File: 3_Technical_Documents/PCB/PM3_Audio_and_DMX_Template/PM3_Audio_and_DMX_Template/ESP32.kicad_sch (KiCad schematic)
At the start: 21 parts, among them SW1 SW_Push, SW2 SW_Push, U1 ESP32-WROOM-32E

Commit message: layout complete
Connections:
- net DIN_1: now also U1.36 (IO22); no longer U1.37 (IO23)
- net DOUT_1: now also U1.37 (IO23); no longer U1.36 (IO22)
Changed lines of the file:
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@@
+		)
+	)
+	(global_label "DIN_1"
+		(shape input)
+		(at 68.58 105.41 0)
+		(fields_autoplaced yes)
+		(effects
+			(font
+				(size 1 1)
+			)
+			(justify left)
+		)
+		(property "Intersheetrefs" "${INTERSHEET_REFS}"
+			(at 75.1684 105.41 0)
+			(effects
+				(font
+					(size 1.27 1.27)
+				)
+				(justify left)
+				(hide yes)
+			)
 		)
 	)
@@
 		)
 	)
+	(global_label "DOUT_1"
+		(shape input)
+		(at 68.58 107.95 0)
+		(fields_autoplaced yes)
+		(effects
+			(font
+				(size 1 1)
+			)
+			(justify left)
+		)
+		(property "Intersheetrefs" "${INTERSHEET_REFS}"
+			(at 76.5017 107.95 0)
+			(effects
+				(font
+					(size 1.27 1.27)
+				)
+				(justify left)
+				(hide yes)
+			)
+		)
+	)
 	(global_label "BCLK_2"
 		(shape input)
@@
 		)
 	)
-	(global_label "DIN_1"
-		(shape input)
-		(at 68.58 107.95 0)
-		(fields_autoplaced yes)
-		(effects
-			(font
-				(size 1 1)
-			)
-			(justify left)
-		)
-		(property "Intersheetrefs" "${INTERSHEET_REFS}"
-			(at 75.1684 107.95 0)
-			(effects
-				(font
-					(size 1.27 1.27)
-				)
-				(justify left)
-				(hide yes)
-			)
-		)
-	)
 	(global_label "Rx"
 		(shape input)
@@
 		)
 	)
-	(global_label "DOUT_1"
-		(shape input)
-		(at 68.58 105.41 0)
-		(fields_autoplaced yes)
-		(effects
-			(font
-				(size 1 1)
-			)
-			(justify left)
-		)
-		(property "Intersheetrefs" "${INTERSHEET_REFS}"
-			(at 76.5017 105.41 0)
-			(effects
-				(font
-					(size 1.27 1.27)
-				)
-				(justify left)
-				(hide yes)
-			)
-		)
-	)
 	(global_label "LRCLK_1"
 		(shape input)
@@
 		)
 		(property "Description" "Push button switch, generic, two pins"
+			(at 228.6 49.53 0)
+			(effects
+				(font
+					(size 1.27 1.27)
+				)
+				(hide yes)
+			)
+		)
+		(property "Sim.Type" ""
 			(at 228.6 49.53 0)
 			(effects
@@
 			)
 		)
+		(property "Sim.Type" ""
+			(at 219.71 44.45 0)
+			(effects
+				(font
+					(size 1.27 1.27)
+				)
+				(hide yes)
+			)
+		)
 		(pin "1"
 		)
@@
 			)
 		)
+		(property "Sim.Type" ""
+			(at 266.7 48.26 0)
+			(effects
+				(font
+					(size 1.27 1.27)
+				)
+				(hide yes)
+			)
+		)
 		(pin "2"
 		)
@@
 			)
 		)
+		(property "Sim.Type" ""
+			(at 156.21 105.41 0)
+			(effects
+				(font
+					(size 1.27 1.27)
+				)
+				(hide yes)
+			)
+		)
 		(pin "2"
 		)
@@
 			)
 		)
+		(property "Sim.Type" ""
+			(at 81.28 92.71 0)
+			(effects
+				(font
+					(size 1.27 1.27)
+				)
+				(hide yes)
+			)
+		)
 		(pin "1"
 		)
@@
 			)
 		)
+		(property "Sim.Type" ""
+			(at 156.21 107.95 0)
+			(effects
+				(font
+					(size 1.27 1.27)
+				)
+				(hide yes)
+			)
+		)
 		(pin "2"
 		)
@@
 			)
 		)
+		(property "Sim.Type" ""
+			(at 156.21 99.06 0)
+			(effects
+				(font
+					(size 1.27 1.27)
+				)
+				(hide yes)
+			)
+		)
 		(pin "2"
 		)
@@
 			)
 		)
+		(property "Sim.Type" ""
+			(at 91.44 43.18 0)
+			(effects
+				(font
+					(size 1.27 1.27)
+				)
+				(hide yes)
+			)
+		)
 		(pin "1"
 		)
@@
 			)
 		)
+		(property "Sim.Type" ""
+			(at 219.71 54.61 0)
+			(effects
+				(font
+					(size 1.27 1.27)
+				)
+				(hide yes)
+			)
+		)
 		(pin "2"
 		)
@@
 			)
 		)
+		(property "Sim.Type" ""
+			(at 257.81 43.18 0)
+			(effects
+				(font
+					(size 1.27 1.27)
+				)
+				(hide yes)
+			)
+		)
 		(pin "1"
 		)
@@
 			)
 		)
+		(property "Sim.Type" ""
+			(at 80.01 43.18 0)
+			(effects
+				(font
+					(size 1.27 1.27)
+				)
+				(hide yes)
+			)
+		)
 		(pin "1"
 		)
@@
 			)
 		)
+		(property "Sim.Type" ""
+			(at 257.81 53.34 0)
+			(effects
+				(font
+					(size 1.27 1.27)
+				)
+				(hide yes)
+			)
+		)
 		(pin "2"
 		)
@@
 			)
 		)
+		(property "Sim.Type" ""
+			(at 156.21 85.09 0)
+			(effects
+				(font
+					(size 1.27 1.27)
+				)
+				(hide yes)
+			)
+		)
 		(pin "2"
 		)
@@
 			)
 		)
+		(property "Sim.Type" ""
+			(at 156.21 93.98 0)
+			(effects
+				(font
+					(size 1.27 1.27)
+				)
+				(hide yes)
+			)
+		)
 		(pin "2"
 		)
@@
 			)
 		)
+		(property "Sim.Type" ""
+			(at 105.41 43.18 0)
+			(effects
+				(font
+					(size 1.27 1.27)
+				)
+				(hide yes)
+			)
+		)
 		(pin "2"
 		)
@@
 			)
 		)
+		(property "Sim.Type" ""
+			(at 156.21 110.49 0)
+			(effects
+				(font
+					(size 1.27 1.27)
+				)
+				(hide yes)
+			)
+		)
 		(pin "2"
 		)
@@
 			)
 		)
+		(property "Sim.Type" ""
+			(at 30.48 35.56 0)
+			(effects
+				(font
+					(size 1.27 1.27)
+				)
+				(hide yes)
+			)
+		)
 		(pin "2"
 		)
@@
 			)
 		)
+		(property "Sim.Type" ""
+			(at 156.21 113.03 0)
+			(effects
+				(font
+					(size 1.27 1.27)
+				)
+				(hide yes)
+			)
+		)
 		(pin "2"
 		)
@@
 			)
 		)
+		(property "Sim.Type" ""
+			(at 156.21 91.44 0)
+			(effects
+				(font
+					(size 1.27 1.27)
+				)
+				(hide yes)
+			)
+		)
 		(pin "2"
 		)
@@
 			)
 		)
+		(property "Sim.Type" ""
+			(at 53.34 97.79 0)
+			(effects
+				(font
+					(size 1.27 1.27)
+				)
+				(hide yes)
+			)
+		)
 		(pin "21"
 		)
@@
 			(at 156.21 96.52 0)
 			(effects
+				(font
+					(size 1.27 1.27)
+				)
+				(hide yes)
+			)
+		)
+		(property "Sim.Type" ""
+			(at 156.21 96.52 0)
+			(effects

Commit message: finalized design and generated gerber
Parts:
- renumbered SW2 to BOOT1, SW1 to EN1
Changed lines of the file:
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@@
 		(dnp no)
 		(fields_autoplaced yes)
-		(property "Reference" "SW1"
+		(property "Reference" "EN1"
 			(at 228.6 41.91 0)
 			(effects
@@
 			(project "PM3_Audio_and_DMX"
 				(path "/1f276d59-ad9b-4e70-a842-f3b7e562eb9b/0cd82055-ce21-4aed-acf2-771a9b05e7c5"
-					(reference "SW1")
+					(reference "EN1")
 					(unit 1)
 				)
@@
 		(dnp no)
 		(fields_autoplaced yes)
-		(property "Reference" "SW2"
+		(property "Reference" "BOOT1"
 			(at 266.7 40.64 0)
 			(effects
@@
 			(project "PM3_Audio_and_DMX"
 				(path "/1f276d59-ad9b-4e70-a842-f3b7e562eb9b/0cd82055-ce21-4aed-acf2-771a9b05e7c5"
-					(reference "SW2")
-					(unit 1)
-				)
+					(reference "BOOT1")
+					(unit 1)
+				)

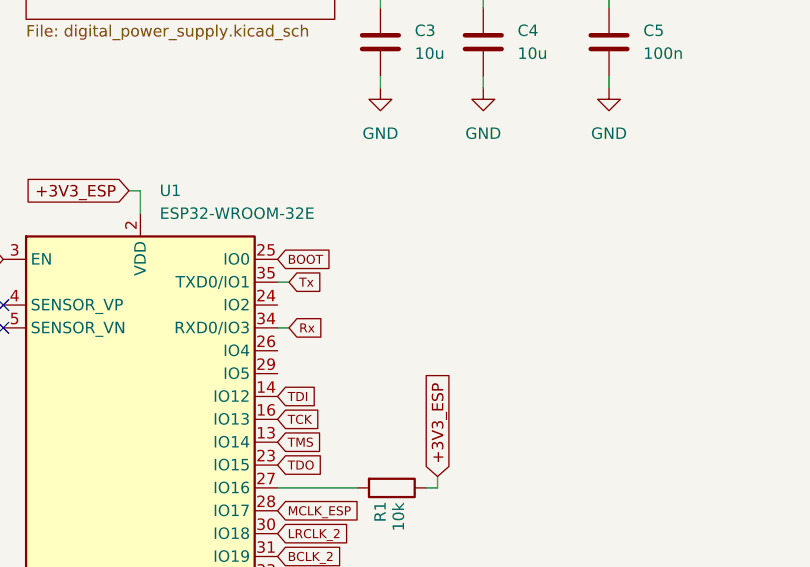
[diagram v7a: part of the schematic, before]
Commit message: forgot programming pins txd rxd esp32
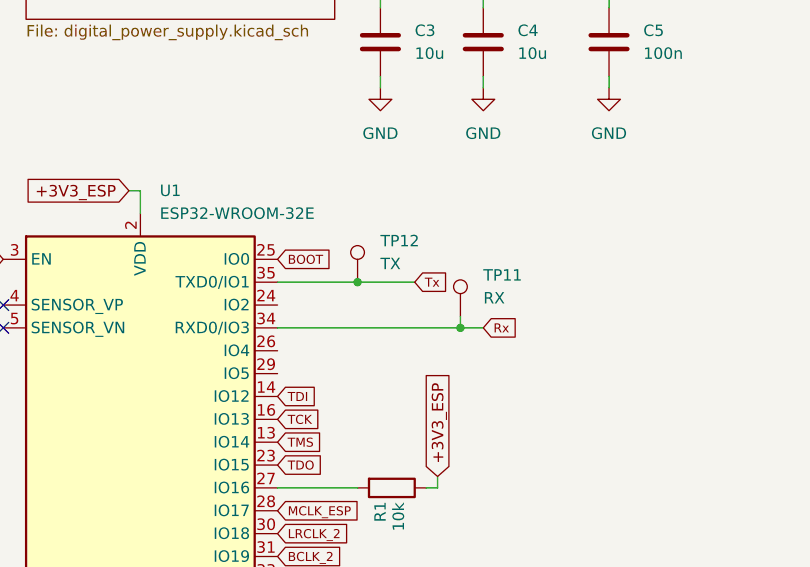
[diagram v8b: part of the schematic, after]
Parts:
- added TP11: RX, symbol Connector:TestPoint
- added TP12: TX, symbol Connector:TestPoint
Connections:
- net Rx: now also TP11.1
- net Tx: now also TP12.1
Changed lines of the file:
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@@
 	)
 	(junction
+		(at 88.9 74.93)
+		(diameter 0)
+		(color 0 0 0 0)
+	)
+	(junction
 		(at 257.81 48.26)
 		(diameter 0)
@@
 		(color 0 0 0 0)
 	)
+	(junction
+		(at 77.47 69.85)
+		(diameter 0)
+		(color 0 0 0 0)
+	)
 	(no_connect
 		(at 38.1 72.39)
@@
 	(wire
 		(pts
+			(xy 77.47 69.85) (xy 68.58 69.85)
+		)
+		(stroke
+			(width 0)
+			(type default)
+		)
+	)
+	(wire
+		(pts
 			(xy 77.47 102.87) (xy 68.58 102.87)
 		)
@@
 	(wire
 		(pts
+			(xy 88.9 73.66) (xy 88.9 74.93)
+		)
+		(stroke
+			(width 0)
+			(type default)
+		)
+	)
+	(wire
+		(pts
 			(xy 80.01 35.56) (xy 80.01 39.37)
 		)
@@
 	(wire
 		(pts
-			(xy 69.85 74.93) (xy 68.58 74.93)
+			(xy 91.44 74.93) (xy 88.9 74.93)
 		)
 		(stroke
@@
 	(wire
 		(pts
-			(xy 69.85 69.85) (xy 68.58 69.85)
+			(xy 83.82 69.85) (xy 77.47 69.85)
 		)
 		(stroke
@@
 	(wire
 		(pts
+			(xy 88.9 74.93) (xy 68.58 74.93)
+		)
+		(stroke
+			(width 0)
+			(type default)
+		)
+	)
+	(wire
+		(pts
 			(xy 160.02 85.09) (xy 163.83 85.09)
 		)
@@
 	(global_label "Tx"
 		(shape input)
-		(at 69.85 69.85 0)
+		(at 83.82 69.85 0)
 		(fields_autoplaced yes)
 		(effects
@@
 		)
 		(property "Intersheetrefs" "${INTERSHEET_REFS}"
-			(at 73.7717 69.85 0)
+			(at 87.7417 69.85 0)
 			(effects
 				(font
@@
 	(global_label "Rx"
 		(shape input)
-		(at 69.85 74.93 0)
+		(at 91.44 74.93 0)
 		(fields_autoplaced yes)
 		(effects
@@
 		)
 		(property "Intersheetrefs" "${INTERSHEET_REFS}"
-			(at 74.0098 74.93 0)
+			(at 95.5998 74.93 0)
 			(effects
 				(font
@@
 	)
 	(symbol
+		(lib_id "Connector:TestPoint")
+		(at 77.47 69.85 0)
+		(unit 1)
+		(exclude_from_sim no)
+		(in_bom yes)
+		(on_board yes)
+		(dnp no)
+		(fields_autoplaced yes)
+		(property "Reference" "TP12"
+			(at 80.01 65.2779 0)
+			(effects
+				(font
+					(size 1.27 1.27)
+				)
+				(justify left)
+			)
+		)
+		(property "Value" "TX"
+			(at 80.01 67.8179 0)
+			(effects
+				(font
+					(size 1.27 1.27)
+				)
+				(justify left)
+			)
+		)
+		(property "Footprint" ""
+			(at 82.55 69.85 0)
+			(effects
+				(font
+					(size 1.27 1.27)
+				)
+				(hide yes)
+			)
+		)
+		(property "Datasheet" "~"
+			(at 82.55 69.85 0)
+			(effects
+				(font
+					(size 1.27 1.27)
+				)
+				(hide yes)
+			)
+		)
+		(property "Description" "test point"
+			(at 77.47 69.85 0)
+			(effects
+				(font
+					(size 1.27 1.27)
+				)
+				(hide yes)
+			)
+		)
+		(pin "1"
+		)
+		(instances
+			(project "PM3_Audio_and_DMX"
+				(path "/1f276d59-ad9b-4e70-a842-f3b7e562eb9b/0cd82055-ce21-4aed-acf2-771a9b05e7c5"
+					(reference "TP12")
+					(unit 1)
+				)
+			)
+		)
+	)
+	(symbol
 		(lib_id "Device:R")
 		(at 219.71 44.45 180)
@@
 					(unit 1)
 				)
+			)
+		)
+	)
+	(symbol
+		(lib_id "Connector:TestPoint")
+		(at 88.9 73.66 0)
+		(unit 1)
+		(exclude_from_sim no)
+		(in_bom yes)
+		(on_board yes)
+		(dnp no)
+		(fields_autoplaced yes)
+		(property "Reference" "TP11"
+			(at 91.44 69.0879 0)
+			(effects
+				(font
+					(size 1.27 1.27)
+				)
+				(justify left)
+			)
+		)
+		(property "Value" "RX"
+			(at 91.44 71.6279 0)
+			(effects
+				(font
+					(size 1.27 1.27)
+				)
+				(justify left)
+			)
+		)
+		(property "Footprint" ""
+			(at 93.98 73.66 0)
+			(effects
+				(font
+					(size 1.27 1.27)
+				)
+				(hide yes)
+			)
+		)
+		(property "Datasheet" "~"
+			(at 93.98 73.66 0)
+			(effects
+				(font
+					(size 1.27 1.27)
+				)
+				(hide yes)
+			)
+		)
+		(property "Description" "test point"
+			(at 88.9 73.66 0)
+			(effects
+				(font
+					(size 1.27 1.27)
+				)
+				(hide yes)
+			)
+		)
+		(pin "1"
+		)
+		(instances
+			(project ""
+				(path "/1f276d59-ad9b-4e70-a842-f3b7e562eb9b/0cd82055-ce21-4aed-acf2-771a9b05e7c5"
+					(reference "TP11")
+					(unit 1)
+				)
